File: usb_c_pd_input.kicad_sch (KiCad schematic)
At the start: 14 parts, among them J1 USB_C_Receptacle, U3 STUSB4500QTR, U4 STL6P3LLH6

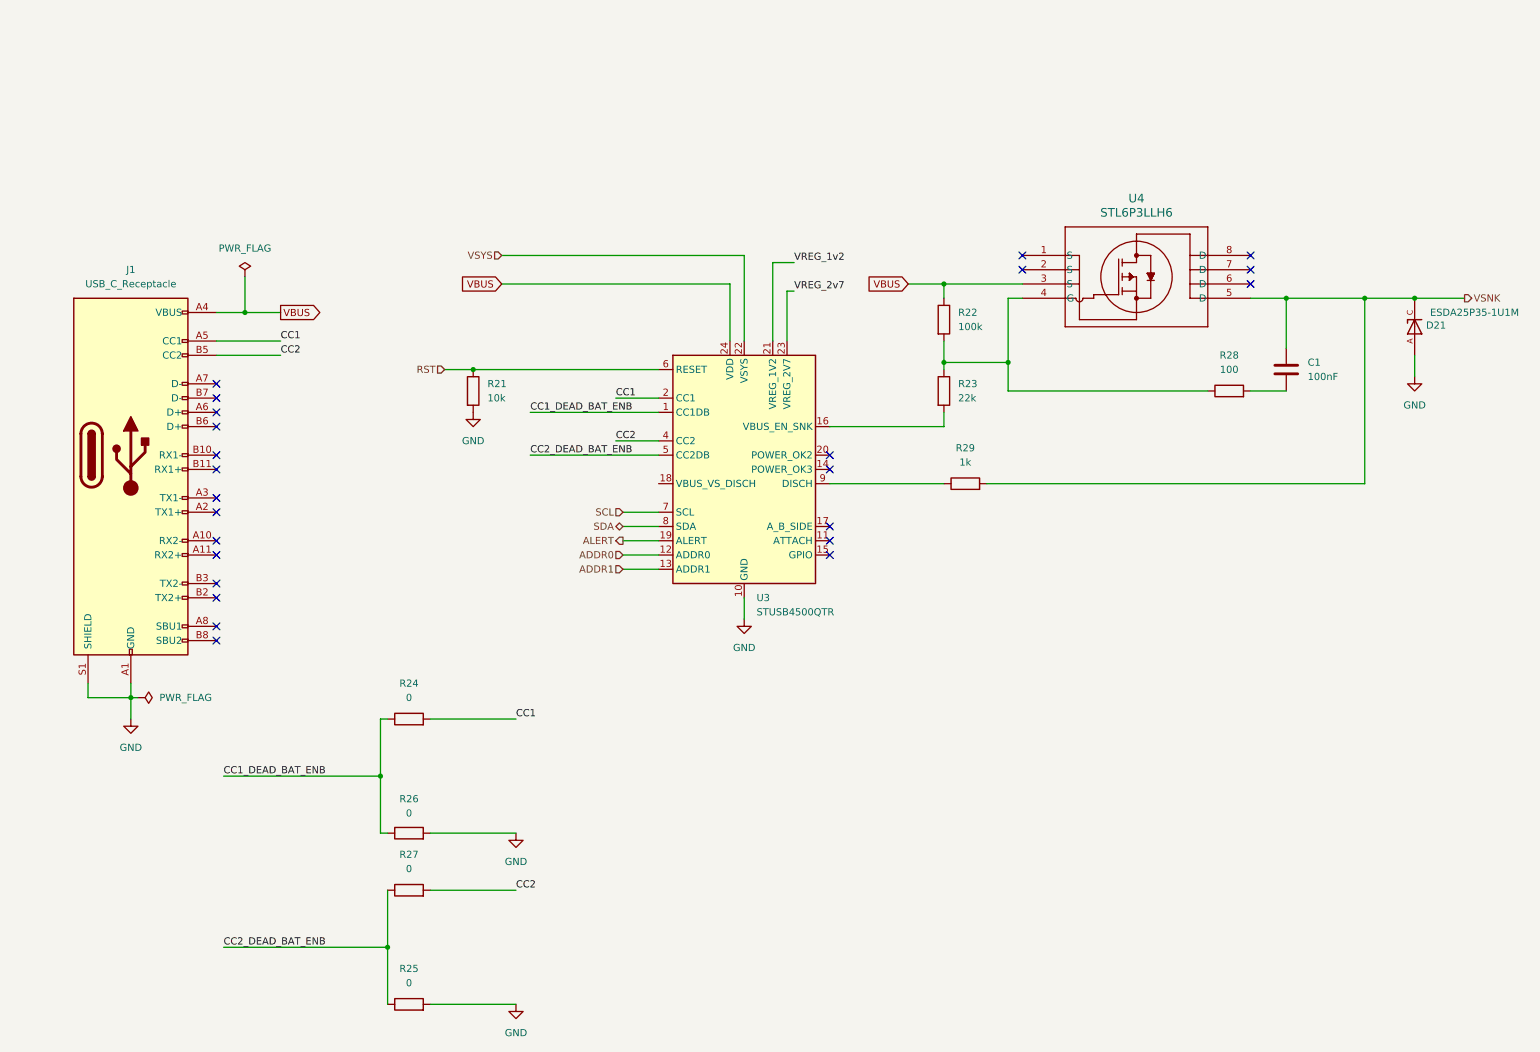
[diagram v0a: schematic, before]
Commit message: Add usb c power + led driver
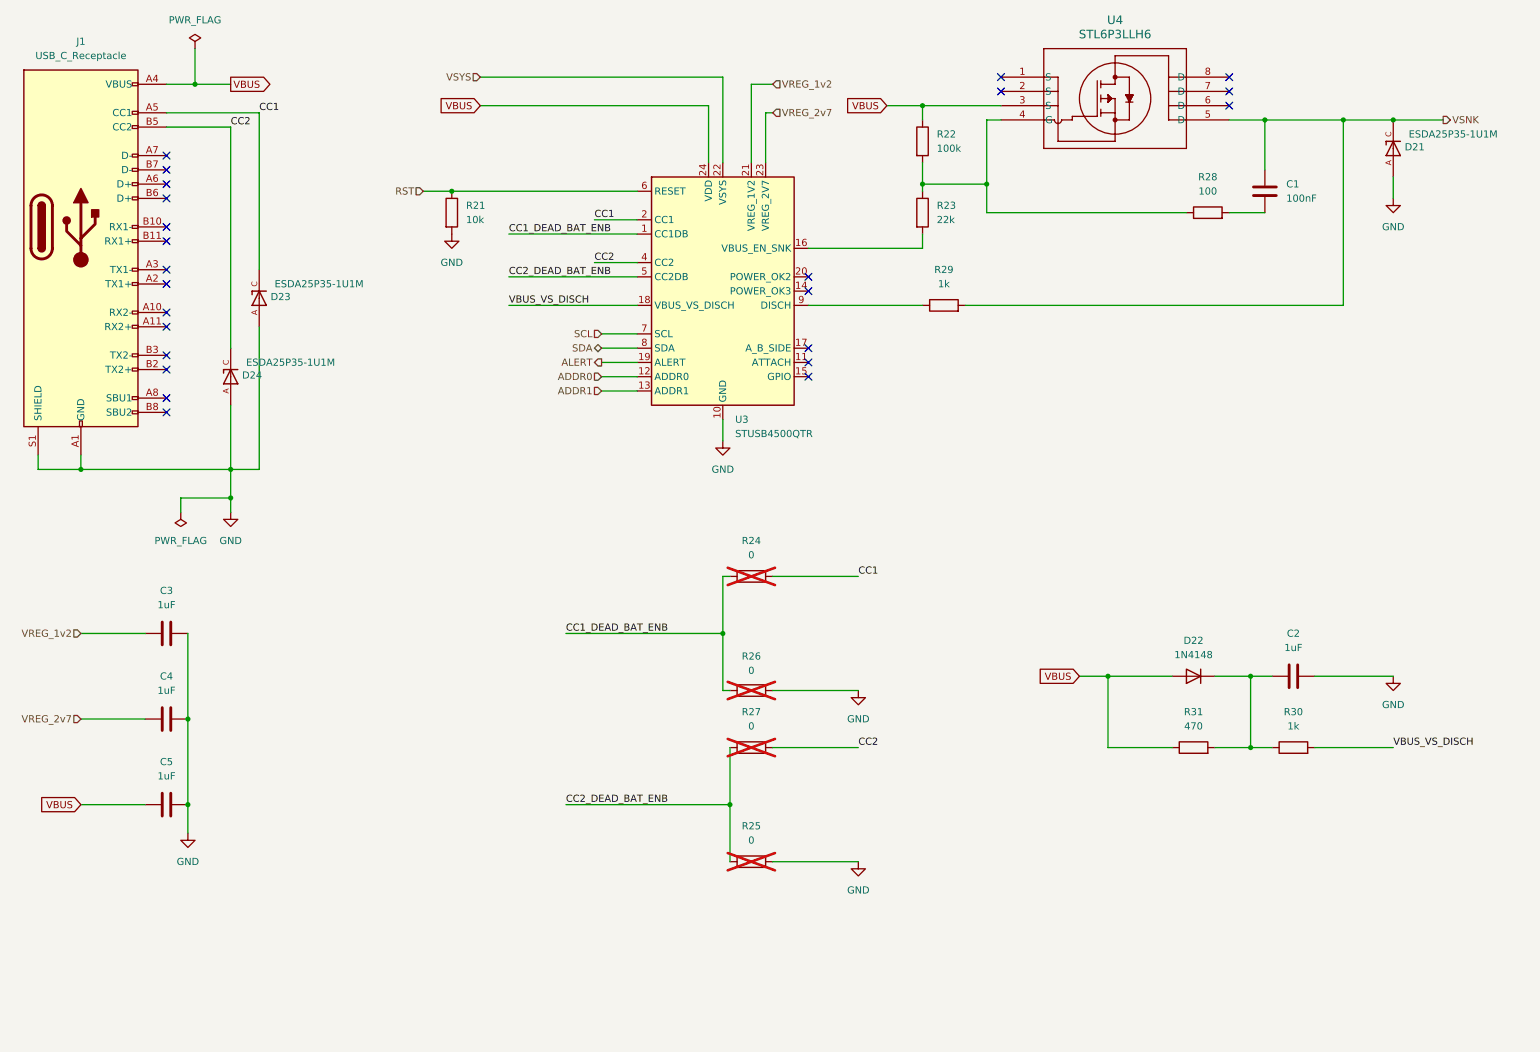
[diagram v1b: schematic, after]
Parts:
- added C2, C3, C4, C5: 1uF, Capacitor_SMD:C_0805_2012Metric, symbol Device:C
- added D22: 1N4148, Diode_THT:D_DO-35_SOD27_P7.62mm_Horizontal, symbol Diode:1N4148
- added D23, D24: ESDA25P35-1U1M, ASethi_Footprints:TVS_ESDA25P35-1U1M, symbol ASethi_Parts:ESDA25P35-1U1M
- added R30: 1k, Resistor_SMD:R_0805_2012Metric, symbol Device:R
- added R31: 470, Resistor_SMD:R_0805_2012Metric, symbol Device:R
- C1: footprint (none) -> Capacitor_SMD:C_0805_2012Metric
- J1: footprint (none) -> Connector_USB:USB_C_Receptacle_HRO_TYPE-C-31-M-17
- R21, R22, R23, R28, R29: footprint (none) -> Resistor_SMD:R_0805_2012Metric
- R24, R25, R26, R27: footprint (none) -> Resistor_SMD:R_0805_2012Metric; now not fitted
- U4: footprint POWERFLAT_3P3X3P3_STM -> ASethi_Footprints:POWERFLAT_3P3X3P3_STM
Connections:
- net CC1: now also D23.C
- net CC2: now also D24.C
- net GND: now also C2.2, C3.2, C4.2, C5.2, D23.A, D24.A
- net VBUS: now also C5.1, D22.2 (A), R31.1
- net VREG_1v2: now also C3.1
- net VREG_2v7: now also C4.1
- net VBUS_VS_DISCH: now reaches U3.18 (VBUS_VS_DISCH)
- net VBUS_VS_DISCH: now also R30.2
- new net: C2.1, D22.1 (K), R30.1, R31.2
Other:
- moved on the sheet: C1, D21, J1, R21, R22, R23, R28, R29, U3, U4

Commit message: Fix ERC
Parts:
- C1, C2, C3, C4, C5: footprint Capacitor_SMD:C_0805_2012Metric -> Capacitor_SMD:C_0805_2012Metric_Pad1.18x1.45mm_HandSolder
- R21, R22, R23, R29, R30: footprint Resistor_SMD:R_0805_2012Metric -> Resistor_SMD:R_0805_2012Metric_Pad1.20x1.40mm_HandSolder
- R24, R25, R26, R27: value 0 -> R; footprint Resistor_SMD:R_0805_2012Metric -> Resistor_SMD:R_0805_2012Metric_Pad1.20x1.40mm_HandSolder
- R28: value 100 -> 100R; footprint Resistor_SMD:R_0805_2012Metric -> Resistor_SMD:R_0805_2012Metric_Pad1.20x1.40mm_HandSolder
- R31: value 470 -> 470R; footprint Resistor_SMD:R_0805_2012Metric -> Resistor_SMD:R_0805_2012Metric_Pad1.20x1.40mm_HandSolder
- U4: footprint ASethi_Footprints:POWERFLAT_3P3X3P3_STM -> POWERFLAT_3P3X3P3_STM
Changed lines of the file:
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@@
 	)
 	(junction
-		(at 46.99 27.94)
-		(diameter 0)
-		(color 0 0 0 0)
-	)
-	(junction
 		(at 237.49 34.29)
 		(diameter 0)
@@
 	)
 	(junction
+		(at 105.41 31.75)
+		(diameter 0)
+		(color 0 0 0 0)
+	)
+	(junction
 		(at 53.34 101.6)
 		(diameter 0)
@@
 	(wire
 		(pts
+			(xy 105.41 31.75) (xy 138.43 31.75)
+		)
+		(stroke
+			(width 0)
+			(type default)
+		)
+	)
+	(wire
+		(pts
 			(xy 140.97 125.73) (xy 140.97 135.89)
 		)
@@
 	(wire
 		(pts
-			(xy 41.91 27.94) (xy 46.99 27.94)
+			(xy 41.91 27.94) (xy 53.34 27.94)
 		)
 		(stroke
@@
 	(wire
 		(pts
-			(xy 97.79 31.75) (xy 138.43 31.75)
+			(xy 97.79 31.75) (xy 105.41 31.75)
 		)
 		(stroke
@@
 	(wire
 		(pts
-			(xy 46.99 21.59) (xy 46.99 27.94)
-		)
-		(stroke
-			(width 0)
-			(type default)
-		)
-	)
-	(wire
-		(pts
 			(xy 246.38 133.35) (xy 260.35 133.35)
 		)
@@
 	(wire
 		(pts
-			(xy 260.35 34.29) (xy 269.24 34.29)
-		)
-		(stroke
-			(width 0)
-			(type default)
-		)
-	)
-	(wire
-		(pts
 			(xy 87.63 46.99) (xy 92.71 46.99)
 		)
@@
 	(wire
 		(pts
-			(xy 46.99 27.94) (xy 53.34 27.94)
-		)
-		(stroke
-			(width 0)
-			(type default)
-		)
-	)
-	(wire
-		(pts
 			(xy 142.24 156.21) (xy 142.24 166.37)
 		)
@@
 	(wire
 		(pts
+			(xy 260.35 34.29) (xy 269.24 34.29)
+		)
+		(stroke
+			(width 0)
+			(type default)
+		)
+	)
+	(wire
+		(pts
 			(xy 45.72 156.21) (xy 45.72 161.29)
 		)
@@
 	)
 	(global_label "VBUS"
-		(shape output)
+		(shape passive)
 		(at 53.34 27.94 0)
 		(fields_autoplaced yes)
@@
 		)
 		(property "Intersheetrefs" "${INTERSHEET_REFS}"
-			(at 61.2238 27.94 0)
+			(at 60.1125 27.94 0)
 			(effects
 				(font
@@
 			)
 		)
-		(property "Footprint" "Capacitor_SMD:C_0805_2012Metric"
+		(property "Footprint" "Capacitor_SMD:C_0805_2012Metric_Pad1.18x1.45mm_HandSolder"
 			(at 45.72 140.0048 0)
 			(effects
@@
 			)
 		)
-		(property "Footprint" "Resistor_SMD:R_0805_2012Metric"
+		(property "Footprint" "Resistor_SMD:R_0805_2012Metric_Pad1.20x1.40mm_HandSolder"
 			(at 180.34 69.088 90)
 			(effects
@@
 	)
 	(symbol
-		(lib_id "power:PWR_FLAG")
-		(at 46.99 21.59 0)
-		(unit 1)
-		(exclude_from_sim no)
-		(in_bom yes)
-		(on_board yes)
-		(dnp no)
-		(fields_autoplaced yes)
-		(property "Reference" "#FLG02"
-			(at 46.99 19.685 0)
-			(effects
-				(font
-					(size 1.27 1.27)
-				)
-				(hide yes)
-			)
-		)
-		(property "Value" "PWR_FLAG"
-			(at 46.99 16.51 0)
-			(effects
-				(font
-					(size 1.27 1.27)
-				)
-			)
-		)
-		(property "Footprint" ""
-			(at 46.99 21.59 0)
-			(effects
-				(font
-					(size 1.27 1.27)
-				)
-				(hide yes)
-			)
-		)
-		(property "Datasheet" "~"
-			(at 46.99 21.59 0)
-			(effects
-				(font
-					(size 1.27 1.27)
-				)
-				(hide yes)
-			)
-		)
-		(property "Description" "Special symbol for telling ERC where power comes from"
-			(at 46.99 21.59 0)
-			(effects
-				(font
-					(size 1.27 1.27)
-				)
-				(hide yes)
-			)
-		)
-		(pin "1"
-		)
-		(instances
-			(project "SwingArm_LEDs"
-				(path "/bf56daef-330a-47b5-9092-f5abcbed14dc/370682c1-3e3f-4a9e-8b49-d84780bf961b"
-					(reference "#FLG02")
-					(unit 1)
-				)
-			)
-		)
-	)
-	(symbol
 		(lib_id "power:GND")
 		(at 140.97 91.44 0)
@@
 			)
 		)
-		(property "Footprint" "Resistor_SMD:R_0805_2012Metric"
+		(property "Footprint" "Resistor_SMD:R_0805_2012Metric_Pad1.20x1.40mm_HandSolder"
 			(at 174.752 38.1 90)
 			(effects
@@
 			)
 		)
-		(property "Footprint" "Resistor_SMD:R_0805_2012Metric"
+		(property "Footprint" "Resistor_SMD:R_0805_2012Metric_Pad1.20x1.40mm_HandSolder"
 			(at 90.932 50.8 90)
 			(effects
@@
 			)
 		)
-		(property "Footprint" "Resistor_SMD:R_0805_2012Metric"
+		(property "Footprint" "Resistor_SMD:R_0805_2012Metric_Pad1.20x1.40mm_HandSolder"
 			(at 174.752 50.8 90)
 			(effects
@@
 	)
 	(symbol
+		(lib_id "power:PWR_FLAG")
+		(at 105.41 31.75 180)
+		(unit 1)
+		(exclude_from_sim no)
+		(in_bom yes)
+		(on_board yes)
+		(dnp no)
+		(fields_autoplaced yes)
+		(property "Reference" "#FLG02"
+			(at 105.41 33.655 0)
+			(effects
+				(font
+					(size 1.27 1.27)
+				)
+				(hide yes)
+			)
+		)
+		(property "Value" "PWR_FLAG"
+			(at 105.41 36.83 0)
+			(effects
+				(font
+					(size 1.27 1.27)
+				)
+			)
+		)
+		(property "Footprint" ""
+			(at 105.41 31.75 0)
+			(effects
+				(font
+					(size 1.27 1.27)
+				)
+				(hide yes)
+			)
+		)
+		(property "Datasheet" "~"
+			(at 105.41 31.75 0)
+			(effects
+				(font
+					(size 1.27 1.27)
+				)
+				(hide yes)
+			)
+		)
+		(property "Description" "Special symbol for telling ERC where power comes from"
+			(at 105.41 31.75 0)
+			(effects
+				(font
+					(size 1.27 1.27)
+				)
+				(hide yes)
+			)
+		)
+		(pin "1"
+		)
+		(instances
+			(project ""
+				(path "/bf56daef-330a-47b5-9092-f5abcbed14dc/370682c1-3e3f-4a9e-8b49-d84780bf961b"
+					(reference "#FLG02")
+					(unit 1)
+				)
+			)
+		)
+	)
+	(symbol
 		(lib_id "ASethi_Parts:ESDA25P35-1U1M")
 		(at 260.35 39.37 270)
@@
 			)
 		)
-		(property "Footprint" "Capacitor_SMD:C_0805_2012Metric"
+		(property "Footprint" "Capacitor_SMD:C_0805_2012Metric_Pad1.18x1.45mm_HandSolder"
 			(at 246.38 132.3848 0)
 			(effects
@@
 			)
 		)
-		(property "Value" "470"
+		(property "Value" "470R"
 			(at 224.79 142.24 90)
 			(effects
@@
 			)
 		)
-		(property "Footprint" "Resistor_SMD:R_0805_2012Metric"
+		(property "Footprint" "Resistor_SMD:R_0805_2012Metric_Pad1.20x1.40mm_HandSolder"
 			(at 224.79 147.828 90)
 			(effects
@@
 			)
 		)
-		(property "Footprint" "Capacitor_SMD:C_0805_2012Metric"
+		(property "Footprint" "Capacitor_SMD:C_0805_2012Metric_Pad1.18x1.45mm_HandSolder"
 			(at 45.72 155.2448 0)
 			(effects
@@
 			)
 		)
-		(property "Value" "0"
+		(property "Value" "R"
 			(at 146.05 162.56 90)
 			(effects
@@
 			)
 		)
-		(property "Footprint" "Resistor_SMD:R_0805_2012Metric"
+		(property "Footprint" "Resistor_SMD:R_0805_2012Metric_Pad1.20x1.40mm_HandSolder"
 			(at 146.05 168.148 90)
 			(effects
@@
 			)
 		)
-		(property "Value" "0"
+		(property "Value" "R"
 			(at 146.05 132.334 90)
 			(effects
@@
 			)
 		)
-		(property "Footprint" "Resistor_SMD:R_0805_2012Metric"
+		(property "Footprint" "Resistor_SMD:R_0805_2012Metric_Pad1.20x1.40mm_HandSolder"
 			(at 146.05 137.668 90)
 			(effects
@@
 			)
 		)
-		(property "Value" "100"
+		(property "Value" "100R"
 			(at 227.33 46.99 90)
 			(effects
@@
 			)
 		)
-		(property "Footprint" "Resistor_SMD:R_0805_2012Metric"
+		(property "Footprint" "Resistor_SMD:R_0805_2012Metric_Pad1.20x1.40mm_HandSolder"
 			(at 227.33 52.578 90)
 			(effects
@@
 			)
 		)
-		(property "Footprint" "ASethi_Footprints:POWERFLAT_3P3X3P3_STM"
+		(property "Footprint" "POWERFLAT_3P3X3P3_STM"
 			(at 190.5 26.67 0)
 			(effects
@@
 			)
 		)
-		(property "Value" "0"
+		(property "Value" "R"
 			(at 146.05 142.24 90)
 			(effects
@@
 			)
 		)
-		(property "Footprint" "Resistor_SMD:R_0805_2012Metric"
+		(property "Footprint" "Resistor_SMD:R_0805_2012Metric_Pad1.20x1.40mm_HandSolder"
 			(at 146.05 147.828 90)
 			(effects
@@
 			)
 		)
-		(property "Footprint" "Resistor_SMD:R_0805_2012Metric"
+		(property "Footprint" "Resistor_SMD:R_0805_2012Metric_Pad1.20x1.40mm_HandSolder"
 			(at 242.57 147.828 90)
 			(effects
@@
 			)
 		)
-		(property "Footprint" "Capacitor_SMD:C_0805_2012Metric"
+		(property "Footprint" "Capacitor_SMD:C_0805_2012Metric_Pad1.18x1.45mm_HandSolder"
 			(at 45.72 124.7648 0)
 			(effects
@@
 			)
 		)
-		(property "Value" "0"
+		(property "Value" "R"
 			(at 146.05 111.76 90)
 			(effects
@@
 			)
 		)
-		(property "Footprint" "Resistor_SMD:R_0805_2012Metric"
+		(property "Footprint" "Resistor_SMD:R_0805_2012Metric_Pad1.20x1.40mm_HandSolder"
 			(at 146.05 117.348 90)
 			(effects
@@
 			)
 		)
-		(property "Footprint" "Capacitor_SMD:C_0805_2012Metric"
+		(property "Footprint" "Capacitor_SMD:C_0805_2012Metric_Pad1.18x1.45mm_HandSolder"
 			(at 238.4552 50.8 0)
 			(effects
